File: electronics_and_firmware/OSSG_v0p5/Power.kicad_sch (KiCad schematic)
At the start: 37 parts, among them J3 USB_B_Micro, Q3 PMZ290UNE2YL, Q4 YJQD30P02A, SW2 Power, U4 XC61CC3002MR, U5 AP5054HTC, U6 MAX17048, U7 NCP167BMX330TBG, U8 SY7088

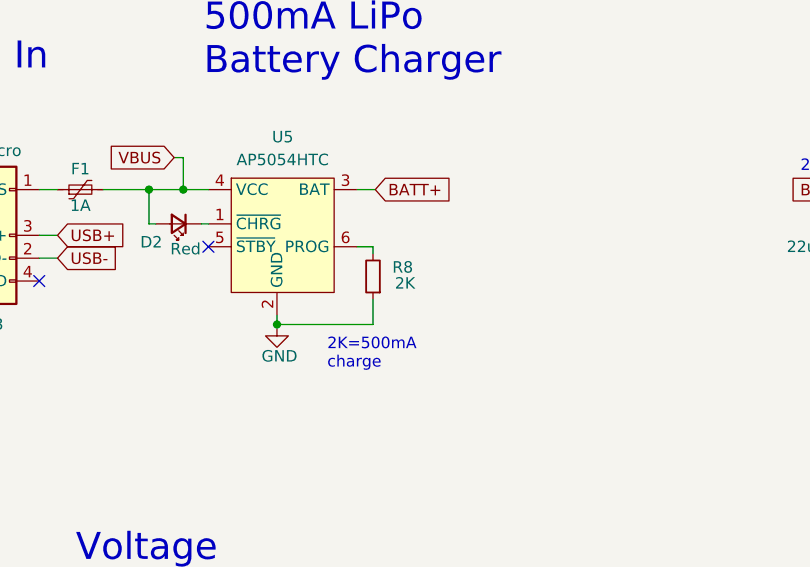
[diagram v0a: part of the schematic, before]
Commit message: fix issues, fix silk screen, add psram pullup, change i2s mic footprint, change battery charging resistor, make notch bigger and fix 3v3 pour not contiguous
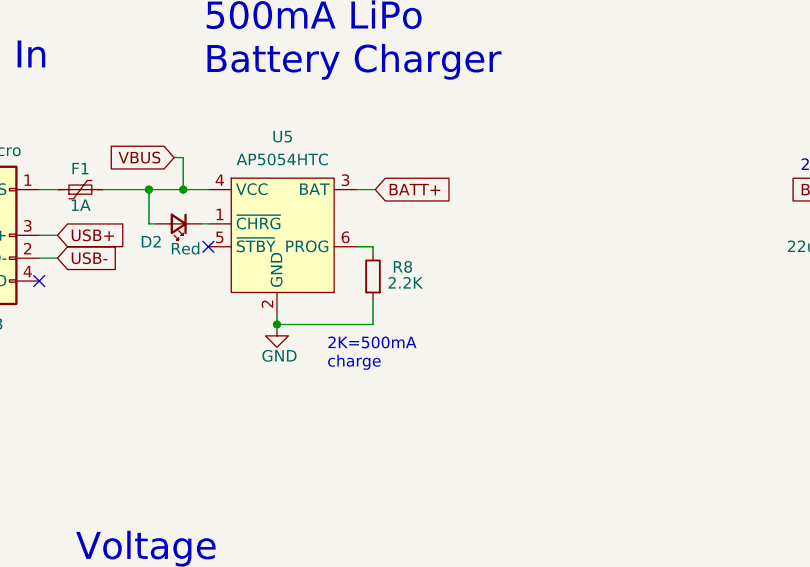
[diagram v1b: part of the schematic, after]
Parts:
- R8: value 2K -> 2.2K
- U5: LCSCLink (none) -> https://www.lcsc.com/product-detail/Battery-Management-ICs_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; MPN_LCSC (none) -> C2843820
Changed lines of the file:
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@@
       (effects (font (size 1.27 1.27)) hide)
     )
-    (property "Datasheet" "" (id 3) (at 80.518 80.01 0)
+    (property "Datasheet" "https://datasheet.lcsc.com/lcsc/2202132030_Wuxi-Chipown-Micro-electronics-AP5054HTCER_C2843820.pdf" (id 3) (at 80.518 80.01 0)
+      (effects (font (size 1.27 1.27)) hide)
+    )
+    (property "MPN_LCSC" "C2843820" (id 4) (at 81.788 67.31 0)
+      (effects (font (size 1.27 1.27)) hide)
+    )
+    (property "LCSCLink" "https://www.lcsc.com/product-detail/Battery-Management-ICs_Wuxi-Chipown-Micro-electronics-AP5054HTCER_C2843820.html" (id 5) (at 81.788 67.31 0)
       (effects (font (size 1.27 1.27)) hide)
     )
@@
     (in_bom yes) (on_board yes)
     (property "Reference" "R8" (id 0) (at 95.758 72.136 0))
-    (property "Value" "2K" (id 1) (at 96.012 73.914 0))
+    (property "Value" "2.2K" (id 1) (at 96.012 73.914 0))
     (property "Footprint" "Resistor_SMD:R_0402_1005Metric" (id 2) (at 92.456 73.152 0)
       (effects (font (size 1.27 1.27)) hide)

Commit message: fill in missing LCSC part numbers (still missing polyfuse
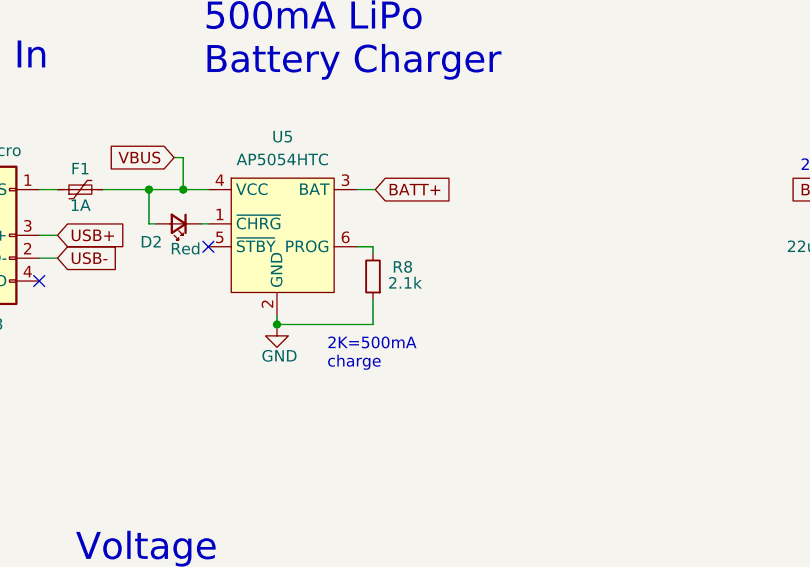
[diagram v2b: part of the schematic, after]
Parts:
- D2: MPN_LCSC (none) -> C965790
- L1: MPN_LCSC (none) -> C241335; P/N C241335 -> (none)
- Q3: MPN_LCSC (none) -> C478155
- Q4: MPN_LCSC (none) -> C919546
- R11, R12: MPN_LCSC 1 -> C2906900; Price_LCSC 0.0005 -> 0.0004
- R13: MPN_LCSC 1 -> C25562; Price_LCSC 0.0005 -> 0.0004
- R14: MPN_LCSC 1 -> C2933073
- R8: value 2.2K -> 2.1k; MPN_LCSC 1 -> C100301; Price_LCSC 0.0005 -> 0.0006
- SW2: MPN_LCSC (none) -> C145858; P/N C145858 -> (none)
- U4: MPN_LCSC (none) -> C80698; MPN_LSCC C80698 -> (none)
- U6: MPN_LCSC (none) -> C2682616; Price_LCSC (none) -> 0.9912
- U8: MPN_LCSC (none) -> C178240
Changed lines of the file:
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@@
       (effects (font (size 1.27 1.27)) hide)
     )
-    (property "MPN_LCSC" "1" (id 4) (at 244.348 66.294 90)
-      (effects (font (size 1.27 1.27)) hide)
-    )
-    (property "Price_LCSC" "0.0005" (id 5) (at 244.348 66.294 90)
+    (property "MPN_LCSC" "C25562" (id 4) (at 244.348 66.294 90)
+      (effects (font (size 1.27 1.27)) hide)
+    )
+    (property "Price_LCSC" "0.0004" (id 5) (at 244.348 66.294 90)
       (effects (font (size 1.27 1.27)) hide)
     )
@@
       (effects (font (size 1.27 1.27)) hide)
     )
-    (property "P/N" "C145858" (id 4) (at 154.178 86.614 0)
+    (property "MPN_LCSC" "C145858" (id 4) (at 154.178 86.614 0)
       (effects (font (size 1.27 1.27)) hide)
     )
@@
       (effects (font (size 1.27 1.27)) hide)
     )
-    (property "P/N" "C241335" (id 4) (at 215.138 63.5 90)
+    (property "MPN_LCSC" "C241335" (id 4) (at 215.138 63.5 90)
       (effects (font (size 1.27 1.27)) hide)
     )
@@
       (effects (font (size 1.27 1.27)) hide)
     )
-    (property "MPN_LCSC" "1" (id 4) (at 244.348 71.882 90)
+    (property "MPN_LCSC" "C2933073" (id 4) (at 244.348 71.882 90)
       (effects (font (size 1.27 1.27)) hide)
     )
@@
     )
     (property "Datasheet" "" (id 3) (at 150.368 132.588 0)
+      (effects (font (size 1.27 1.27)) hide)
+    )
+    (property "MPN_LCSC" "C2682616" (id 4) (at 150.368 132.588 0)
+      (effects (font (size 1.27 1.27)) hide)
+    )
+    (property "Price_LCSC" "0.9912" (id 5) (at 150.368 132.588 0)
       (effects (font (size 1.27 1.27)) hide)
     )
@@
       (effects (font (size 1.27 1.27)) hide)
     )
+    (property "MPN_LCSC" "C178240" (id 4) (at 229.362 67.31 0)
+      (effects (font (size 1.27 1.27)) hide)
+    )
     (pin "1")
     (pin "2")
@@
       (effects (font (size 1.27 1.27)) hide)
     )
+    (property "MPN_LCSC" "C919546" (id 4) (at 182.626 66.04 90)
+      (effects (font (size 1.27 1.27)) hide)
+    )
     (pin "1")
     (pin "2")
@@
       (effects (font (size 1.27 1.27)) hide)
     )
-    (property "MPN_LCSC" "1" (id 4) (at 184.404 78.74 90)
-      (effects (font (size 1.27 1.27)) hide)
-    )
-    (property "Price_LCSC" "0.0005" (id 5) (at 184.404 78.74 90)
+    (property "MPN_LCSC" "C2906900" (id 4) (at 184.404 78.74 90)
+      (effects (font (size 1.27 1.27)) hide)
+    )
+    (property "Price_LCSC" "0.0004" (id 5) (at 184.404 78.74 90)
       (effects (font (size 1.27 1.27)) hide)
     )
@@
       (effects (font (size 1.27 1.27)) hide)
     )
+    (property "MPN_LCSC" "C478155" (id 4) (at 167.386 77.724 0)
+      (effects (font (size 1.27 1.27)) hide)
+    )
     (pin "1")
     (pin "2")
@@
     )
     (property "Datasheet" "~" (id 3) (at 169.926 64.77 0)
+      (effects (font (size 1.27 1.27)) hide)
+    )
+    (property "MPN_LCSC" "C919546" (id 4) (at 169.926 66.04 90)
       (effects (font (size 1.27 1.27)) hide)
     )
@@
       (effects (font (size 1.27 1.27)) hide)
     )
-    (property "MPN_LSCC" "C80698" (id 4) (at 68.58 128.27 0)
+    (property "MPN_LCSC" "C80698" (id 4) (at 68.58 128.27 0)
       (effects (font (size 1.27 1.27)) hide)
     )
@@
       (effects (font (size 1.27 1.27)) hide)
     )
-    (property "MPN_LCSC" "1" (id 4) (at 163.068 67.564 90)
-      (effects (font (size 1.27 1.27)) hide)
-    )
-    (property "Price_LCSC" "0.0005" (id 5) (at 163.068 67.564 90)
+    (property "MPN_LCSC" "C2906900" (id 4) (at 163.068 67.564 90)
+      (effects (font (size 1.27 1.27)) hide)
+    )
+    (property "Price_LCSC" "0.0004" (id 5) (at 163.068 67.564 90)
       (effects (font (size 1.27 1.27)) hide)
     )
@@
     (in_bom yes) (on_board yes)
     (property "Reference" "R8" (id 0) (at 95.758 72.136 0))
-    (property "Value" "2.2K" (id 1) (at 96.012 73.914 0))
+    (property "Value" "2.1k" (id 1) (at 96.012 73.914 0))
     (property "Footprint" "Resistor_SMD:R_0402_1005Metric" (id 2) (at 92.456 73.152 0)
       (effects (font (size 1.27 1.27)) hide)
@@
       (effects (font (size 1.27 1.27)) hide)
     )
-    (property "MPN_LCSC" "1" (id 4) (at 92.456 73.152 90)
-      (effects (font (size 1.27 1.27)) hide)
-    )
-    (property "Price_LCSC" "0.0005" (id 5) (at 92.456 73.152 90)
+    (property "MPN_LCSC" "C100301" (id 4) (at 92.456 73.152 90)
+      (effects (font (size 1.27 1.27)) hide)
+    )
+    (property "Price_LCSC" "0.0006" (id 5) (at 92.456 73.152 90)
       (effects (font (size 1.27 1.27)) hide)
     )
@@
       (effects (font (size 1.27 1.27)) hide)
     )
+    (property "MPN_LCSC" "C965790" (id 4) (at 70.866 67.31 0)
+      (effects (font (size 1.27 1.27)) hide)
+    )

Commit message: final v0.5 PCB and components order files
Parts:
- F1: MPN_LCSC (none) -> C2830233
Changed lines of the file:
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@@
+      (effects (font (size 1.27 1.27)) hide)
+    )
+    (property "MPN_LCSC" "C2830233" (id 4) (at 59.944 63.5 90)
       (effects (font (size 1.27 1.27)) hide)
     )

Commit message: updated KiCAD V0.4 and V0.5 schematics with correct switch part number
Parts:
- SW2: MPN_LCSC C145858 -> C145857
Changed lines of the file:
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@@
       (effects (font (size 1.27 1.27)) hide)
     )
-    (property "MPN_LCSC" "C145858" (id 4) (at 154.178 86.614 0)
+    (property "MPN_LCSC" "C145857" (id 4) (at 154.178 86.614 0)
       (effects (font (size 1.27 1.27)) hide)
     )
